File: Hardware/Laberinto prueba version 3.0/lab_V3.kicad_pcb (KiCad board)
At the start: 2 copper layers, 100 x 100 mm, 27 parts, among them J1 MotorIzq, J10 DRV8833_IN, J11 DRV8833_OUT, J2 MotorDer, J3 SWITCH, J4 Jack_Batt, J5 Distancia_Izq, J6 Distancia_Frontal, J7 Distancia_Der, J8 Encoder_DER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

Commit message: continuamos PCB
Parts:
- moved U2 119.4 mm to (159.5, 78.0)
- moved C1 113.3 mm to (121.3, 99.5), turned to 0 degrees
- moved R2 104.5 mm to (159.5, 73.0), turned to 0 degrees
- moved R1 103.9 mm to (128.5, 81.5)
- moved R3 100.8 mm to (165.0, 73.0)
- moved U1 84.0 mm to (128.0, 99.5), turned to 0 degrees
- moved SW2 73.7 mm to (195.5, 73.5), turned to -90 degrees
- moved SW1 73.7 mm to (195.5, 82.5), turned to -90 degrees
- moved C4 52.0 mm to (128.6, 87.0)
- moved C2 51.7 mm to (121.2, 95.7), turned to 0 degrees
- moved C3 49.8 mm to (129.0, 91.0), turned to 0 degrees
- moved Display1 49.6 mm to (286.0, 42.5)
- moved LED1 33.2 mm to (123.5, 83.8), turned to -90 degrees
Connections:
- U3 pad 10: /D1 -> /Strategy_A
- U3 pad 8: /start -> /Start
- U3 pad 9: /Strategy_A -> /D1
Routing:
- net GND: track 0.00 -> 95.6 mm
- net /IR_FRONTAL: track 20.1 -> 30.3 mm
- net /IR_DER: track 38.7 -> 48.4 mm
- net +5V: track 99.6 -> 100.5 mm
- added copper zone on B.Cu, net GND

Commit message: sch cambio2
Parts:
- removed J8: Encoder_DER, Connector_JST:JST_EH_B4B-EH-A_1x04_P2.50mm_Vertical
- removed J9: Encoder_IZQ, Connector_JST:JST_EH_B4B-EH-A_1x04_P2.50mm_Vertical
- removed SW2: SW_Push, EESTN5:Pulsador_TH_4
- J1: value MotorIzq -> Encoder Derecho; footprint Connector_JST:JST_EH_B2B-EH-A_1x02_P2.50mm_Vertical -> EESTN5:pin_strip_6
- J2: value MotorDer -> Encoder Izquierdo; footprint Connector_JST:JST_EH_B2B-EH-A_1x02_P2.50mm_Vertical -> EESTN5:pin_strip_6
- moved J2 24.7 mm to (198.3, 106.0), turned to 180 degrees
- moved J1 7.40 mm to (139.8, 108.0), turned to 180 degrees
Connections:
- J1 pad 1: /BOUT2 -> /AOUT1
- J1 pad 2: /BOUT1 -> /AOUT2
- J2 pad 1: /AOUT1 -> /BOUT2
- J2 pad 2: /AOUT2 -> /BOUT1
- U3 pad 10: /Strategy_A -> /D1A
- U3 pad 26: /D0 -> /D2A
- U3 pad 9: /D1 -> /D1B
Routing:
- net /D0: track 45.8 -> 0.00 mm
- net /D2A: track 0.00 -> 28.9 mm

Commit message: Placa lista solo faltan alguna correcciones de taiel
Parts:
- J1, J2: footprint EESTN5:pin_strip_6 -> Connector_JST:JST_EH_B6B-EH-A_1x06_P2.50mm_Vertical
- LED1: footprint EESTN5:LED_1206 -> EESTN5:led_5mm_green
- moved Display1 134.7 mm to (157.6, 83.2), turned to 180 degrees
- moved J1 12.4 mm to (127.4, 107.4), turned to 0 degrees
- moved U1 9.36 mm to (128.8, 90.2)
- moved C1 9.10 mm to (121.9, 90.4)
- moved C2 8.36 mm to (121.9, 87.4)
- moved C3 7.69 mm to (128.9, 83.3)
- moved C4 7.31 mm to (128.9, 79.7)
- moved J6 7.05 mm to (157.5, 53.9)
- moved LED1 5.85 mm to (124.0, 77.9), turned to 180 degrees
- moved J2 5.48 mm to (193.0, 107.2)
- moved R1 5.32 mm to (128.9, 76.2)
- moved R3 1.55 mm to (166.5, 73.4)
- moved R2 1.54 mm to (161.0, 73.4)
- moved U2 0.71 mm to (160.0, 77.5)
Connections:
- J11 pad 2: /BOUT1 -> /AOUT2
- J11 pad 3: /BOUT2 -> /AOUT1
- J11 pad 4: /AOUT2 -> /BOUT1
- J11 pad 5: /AOUT1 -> /BOUT2
- J2 pad 1: /BOUT2 -> /BOUT1
- J2 pad 2: /BOUT1 -> /BOUT2
- U3 pad 10: /D1A -> /IR_DER
- U3 pad 24: /AIN1 -> /AIN2
- U3 pad 25: /AIN2 -> /AIN1
- U3 pad 3: unconnected-(U3-Pad3) -> /Start
- U3 pad 4: /IR_FRONTAL -> /IR_IZQ
- U3 pad 5: /IR_IZQ -> /IR_FRONTAL
- U3 pad 6: /IR_DER -> /TATAMI
- U3 pad 7: /TATAMI -> /D2B
- U3 pad 8: /Start -> /D1B
- U3 pad 9: /D1B -> /D1A
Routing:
- net +5V: track 100.5 -> 328.8 mm, vias 0 -> 2
- net /D2B: track 0.00 -> 97.7 mm
- net +BATT: track 4.70 -> 78.8 mm, vias 0 -> 2
- net GND: track 95.6 -> 28.9 mm, vias 0 -> 4
- net /D1B: track 0.00 -> 55.3 mm
- net /D1A: track 0.00 -> 55.2 mm
- net /BOUT1: track 12.7 -> 52.6 mm
- net /Start: track 0.00 -> 35.2 mm
- net /AOUT1: track 13.9 -> 47.8 mm
- net /BOUT2: track 16.0 -> 43.9 mm
- net /AOUT2: track 17.3 -> 40.4 mm
- net /TATAMI: track 0.00 -> 21.2 mm
- net /AIN1: track 15.5 -> 33.4 mm
- net /IR_DER: track 48.4 -> 30.8 mm
- net /IR_FRONTAL: track 30.3 -> 13.5 mm
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
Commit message: estamos haciendo la placa ya
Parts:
- added BoBer: LOGO, EESTN5:LOGO_BOVER_SER, F.Cu at (159.0, 131.0)
- added G***: LOGO, EESTN5:LOGO_BOVER_SER, F.Cu at (203.0, 104.0)
- J4: value Jack_Batt -> Alimentacion
- J5: value Distancia_Izq -> Sensor Izquierdo
- J6: value Distancia_Frontal -> Sensor Frontal
- J7: value Distancia_Der -> Sensor Derecha
- LED1: moved to F.Cu
- Start1: renamed from SW1; value SW_Push -> Start
- turned LED1 to 0 degrees
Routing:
- net GND: track 28.9 -> 23.5 mm
- net +5V: track 328.8 -> 328.3 mm

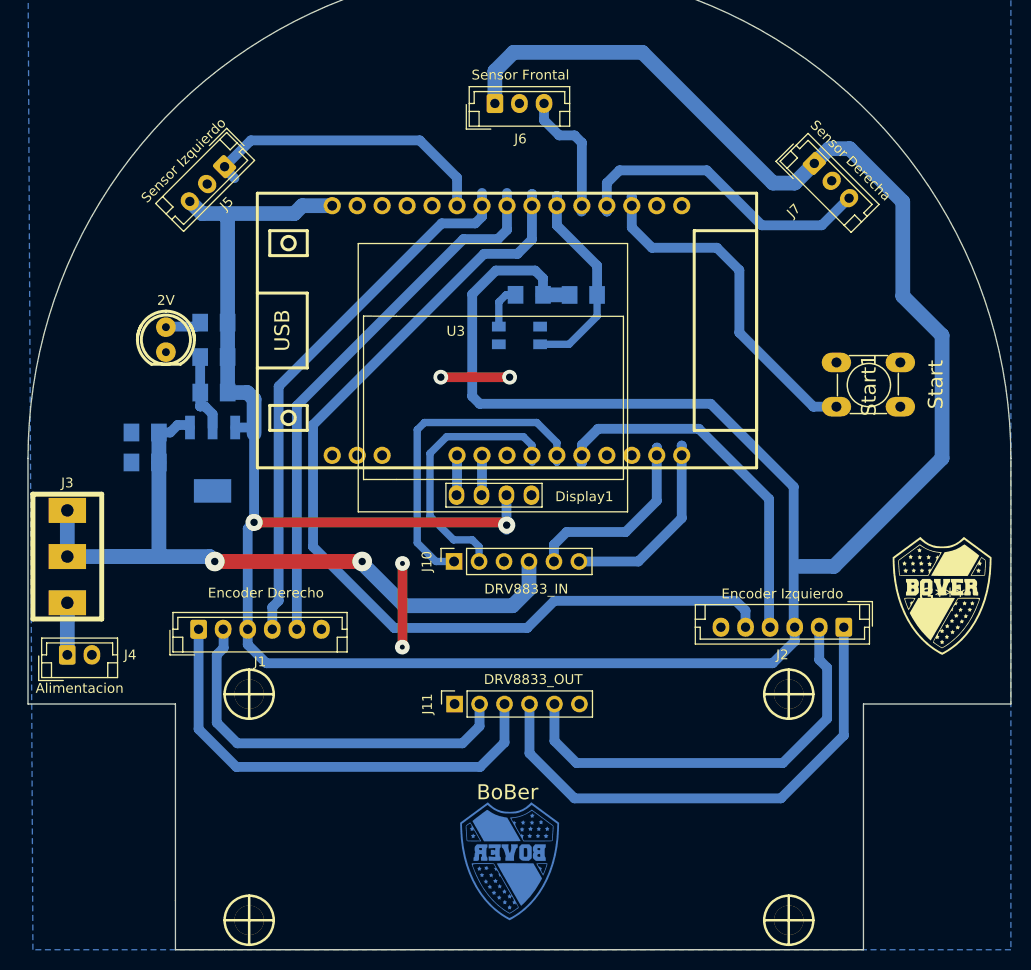
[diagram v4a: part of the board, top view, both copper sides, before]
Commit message: cambios en el diseño 3d de soportes IR
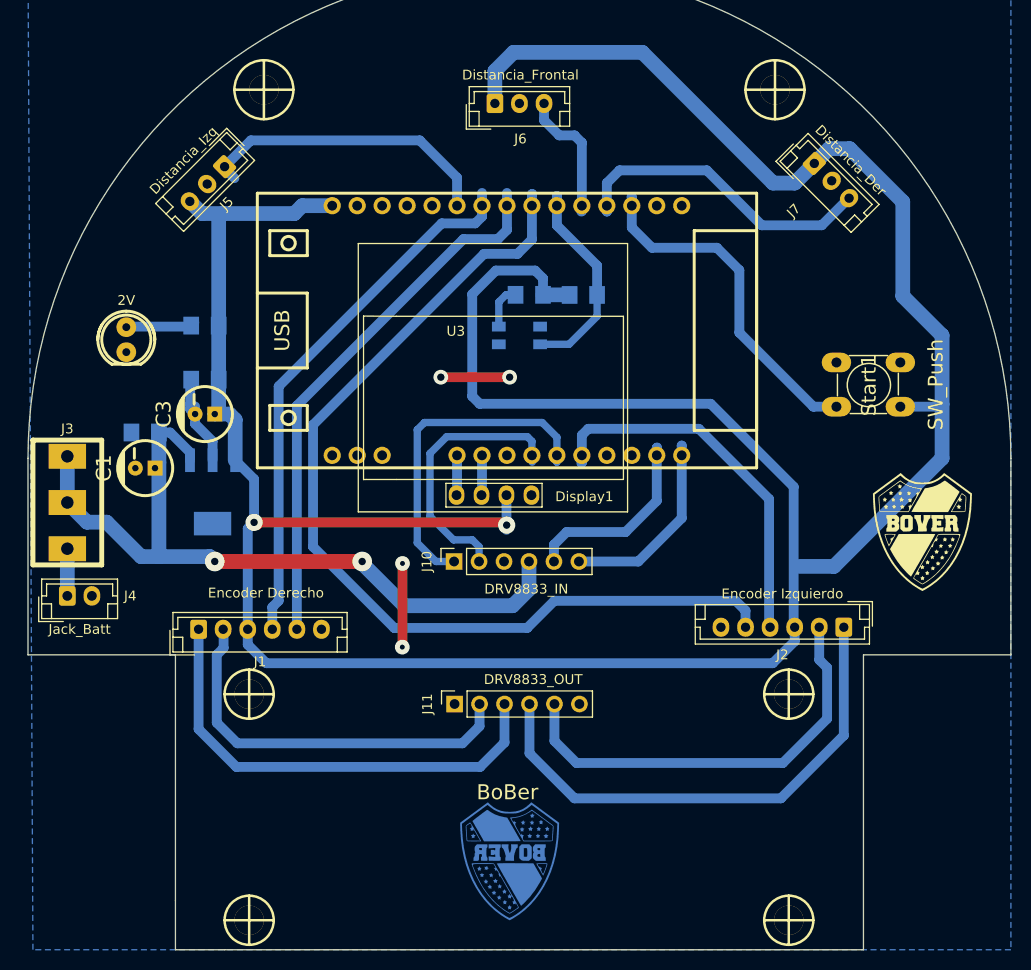
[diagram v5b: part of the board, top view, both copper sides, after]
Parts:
- added hole_3mm: VAL**, EESTN5:hole_3mm, F.Cu at (186.0, 52.5)
- added hole_3mm: VAL**, EESTN5:hole_3mm, F.Cu at (134.0, 52.5)
- C1: footprint EESTN5:C_1206 -> EESTN5:CAP_ELEC_5x11mm; moved to F.Cu
- C3: value 10uF -> 220uF; footprint EESTN5:C_1206 -> EESTN5:CAP_ELEC_5x11mm; moved to F.Cu
- J4: value Alimentacion -> Jack_Batt
- J5: value Sensor Izquierdo -> Distancia_Izq
- J6: value Sensor Frontal -> Distancia_Frontal
- J7: value Sensor Derecha -> Distancia_Der
- Start1: value Start -> SW_Push
- moved G*** 6.80 mm to (201.0, 97.5)
- moved J4 6.00 mm to (114.0, 104.0)
- moved J3 5.50 mm to (114.0, 94.5)
- moved LED1 4.03 mm to (120.0, 77.9)
- moved U1 3.33 mm to (128.8, 93.5)
- moved C4 2.47 mm to (128.0, 82.0)
- moved C3 2.37 mm to (128.0, 85.5), turned to 90 degrees
- moved R1 0.96 mm to (128.0, 76.5)
- moved C1 0.58 mm to (121.9, 91.0), turned to 90 degrees
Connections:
- Start1 pad 1: GND -> +5V
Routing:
- net Net-(LED1-Pad1): track 3.70 -> 7.12 mm
- net GND: track 23.5 -> 26.7 mm
- net +5V: track 328.3 -> 330.8 mm
- net +BATT: track 78.6 -> 77.1 mm
- net /D2A: track 37.6 -> 38.2 mm
- net /VBAT: track 5.30 -> 4.80 mm
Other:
- outline, holes or cut-outs redrawn
